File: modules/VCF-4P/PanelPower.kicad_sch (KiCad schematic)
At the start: 33 parts, among them J1 WQP-PJ398, J10 Conn_Front_Left, J11 Conn_Back_Right, J12 Conn_Front_Right, J13 Conn_Back_Left, J3 WQP-PJ398, J4 WQP-PJ398, J5 WQP-PJ398, J7 WQP-PJ398, J9 Conn_Eurorack_16, U2 TL074

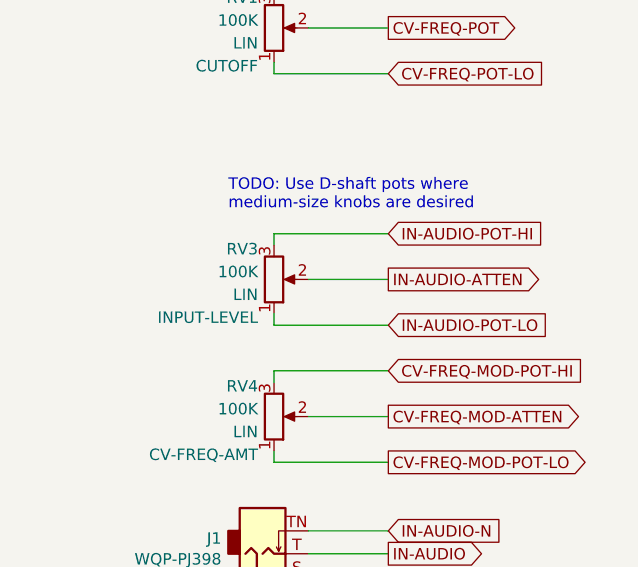
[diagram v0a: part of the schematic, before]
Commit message: VCF-4P: input level uses audio-taper pot
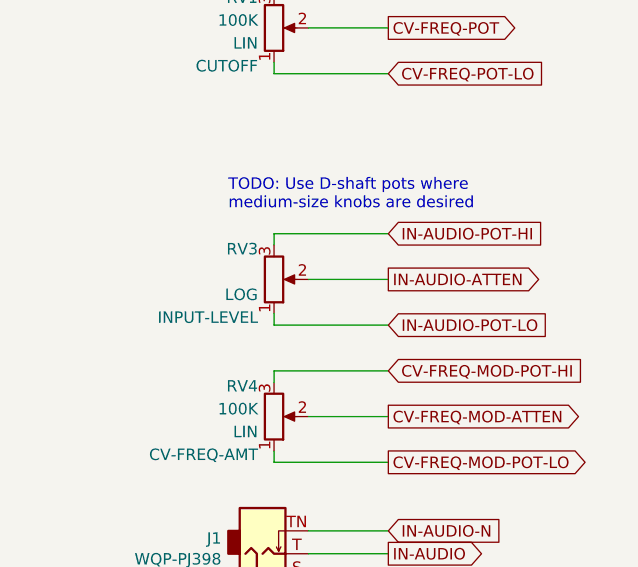
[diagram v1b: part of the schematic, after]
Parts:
- RV3: value 100K -> (none); footprint -lmp-synth:Potentiometer_Alpha_RD901F-40-00D_Single_Vertical -> (none); Value2 LIN -> LOG

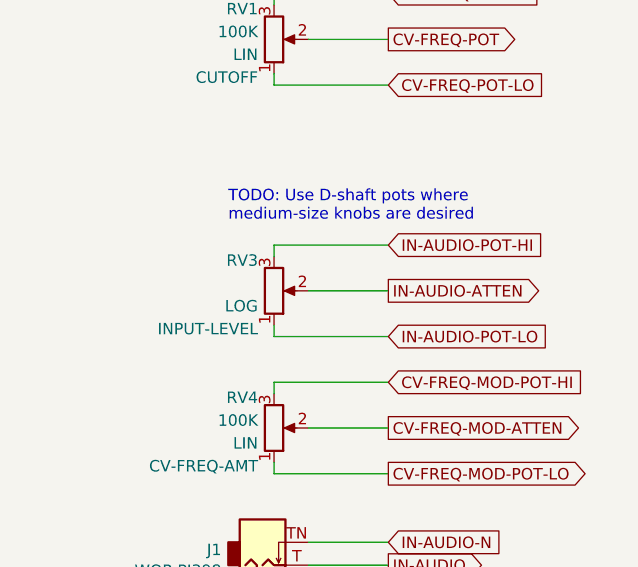
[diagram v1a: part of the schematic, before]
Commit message: VCF-4P: Breadboard prototype - wip
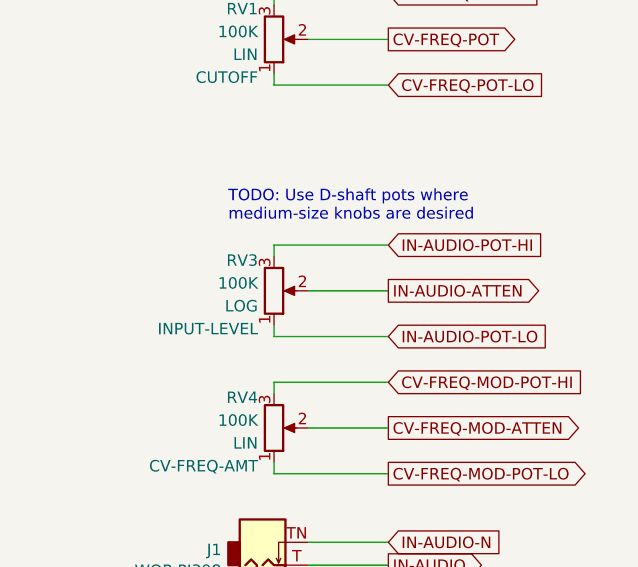
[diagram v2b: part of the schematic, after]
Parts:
- RV3: value (none) -> 100K; footprint (none) -> -lmp-synth:Potentiometer_Alpha_RD901F-40-00D_Single_Vertical

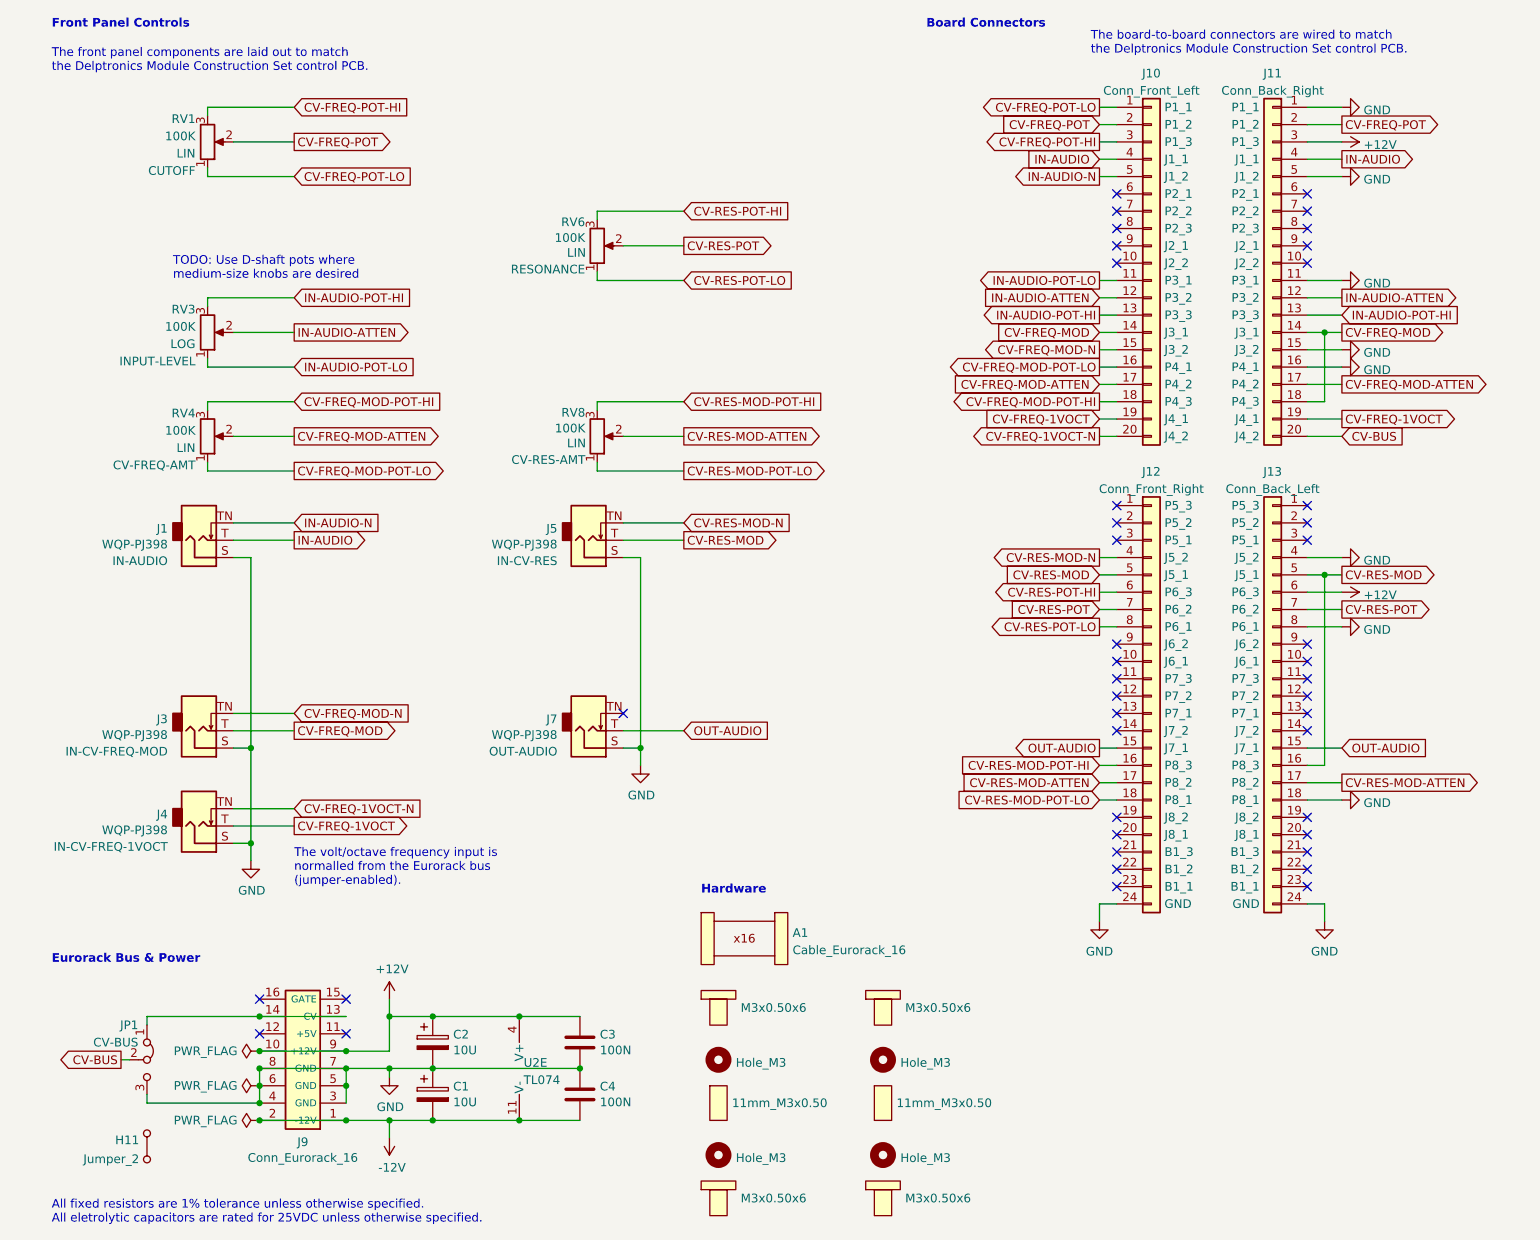
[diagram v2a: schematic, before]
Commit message: VCF-4P: Correct part numbers for DIP breakout version of SSI2140
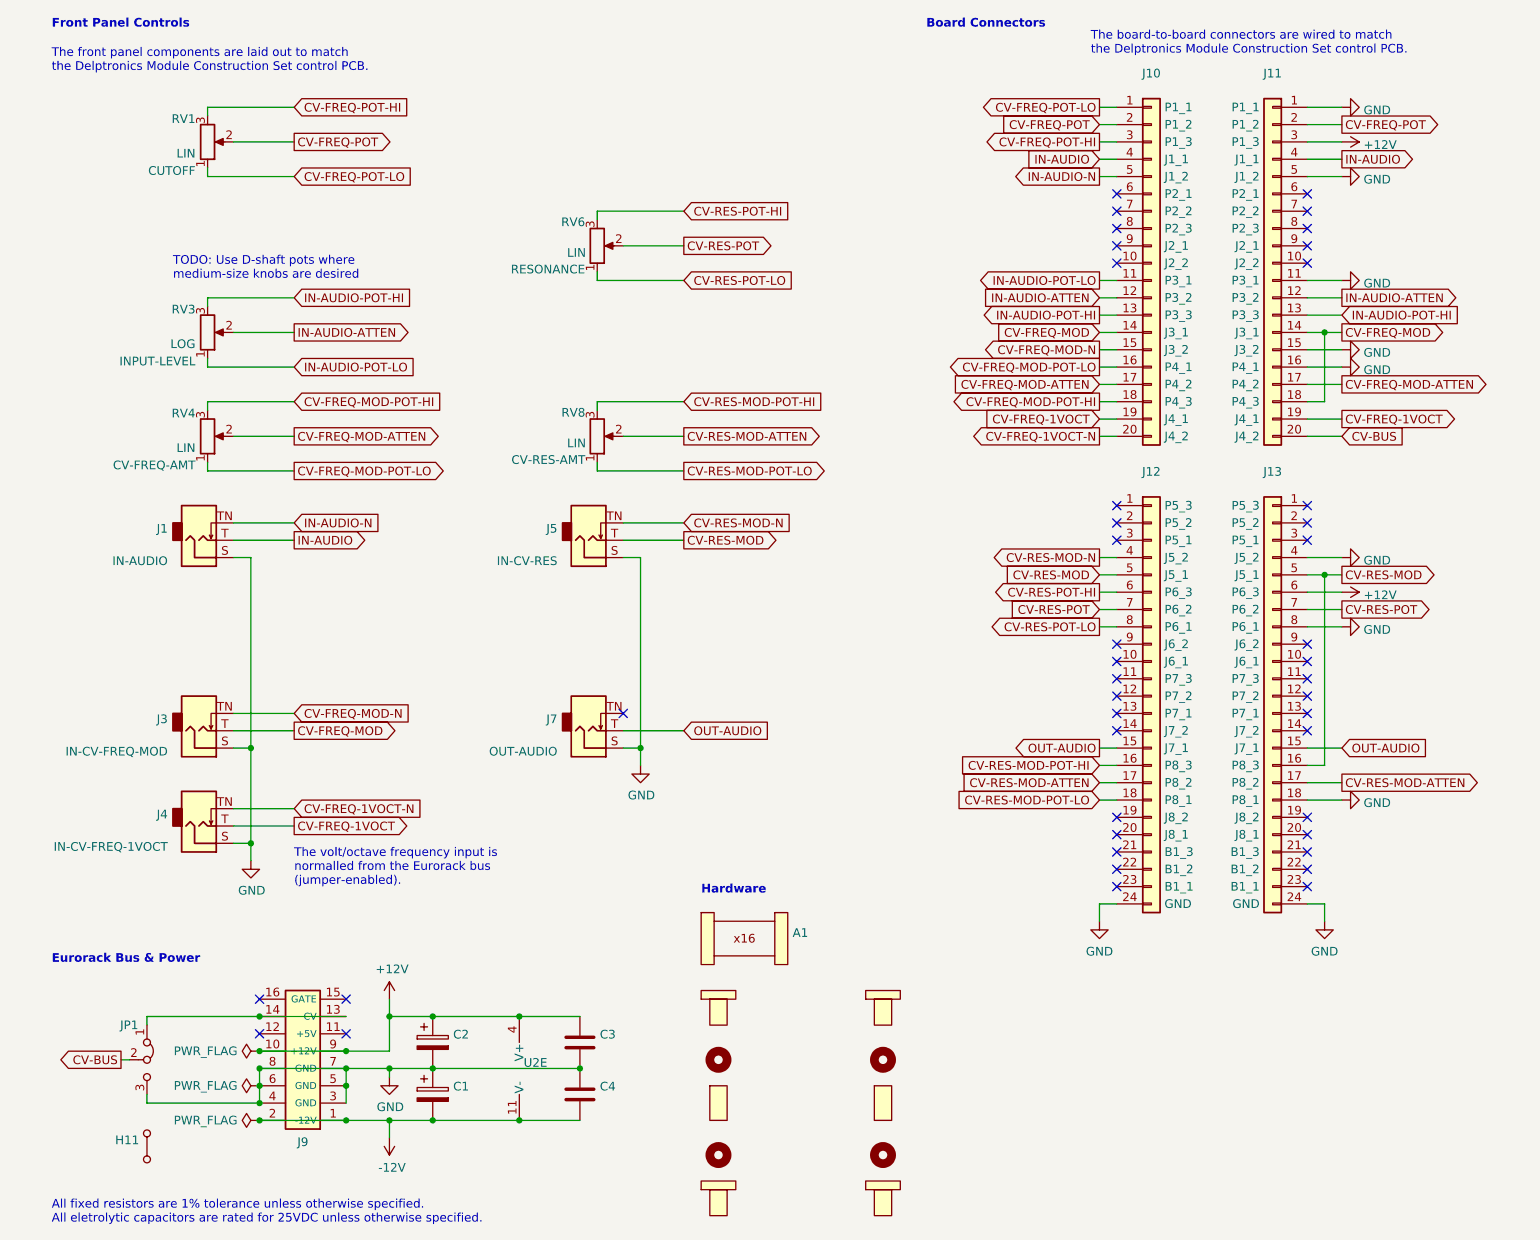
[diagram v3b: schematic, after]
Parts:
- A1: value Cable_Eurorack_16 -> (none); footprint -lmp-misc:NoFootprint -> (none)
- C1, C2: value 10U -> (none); footprint -lmp-misc:CP_Radial_D4.0mm_P1.50mm -> (none)
- C3, C4: value 100N -> (none); footprint -lmp-misc:C_Disc_D5.0mm_W2.5mm_P2.50mm -> (none)
- H1, H2, H3, H4: value Hole_M3 -> (none); footprint -lmp-holes:MountingHole_PCB_3.2mm_M3 -> (none)
- H10, H5, H7, H8: value M3x0.50x6 -> (none)
- H11: value Jumper_2 -> (none); footprint -lmp-misc:NoFootprint -> (none)
- H6, H9: value 11mm_M3x0.50 -> (none)
- J1, J3, J4, J5, J7: value WQP-PJ398 -> (none); footprint -lmp-synth:Jack_3.5mm_QingPu_WQP-PJ398SM_Vertical -> (none)
- J10: value Conn_Front_Left -> (none); footprint -lmp-synth:PinSocket_Delptronics_Front -> (none)
- J11: value Conn_Back_Right -> (none); footprint -lmp-synth:PinHeader_Delptronics_Back_8HP -> (none)
- J12: value Conn_Front_Right -> (none); footprint -lmp-synth:PinSocket_Delptronics_Front -> (none)
- J13: value Conn_Back_Left -> (none); footprint -lmp-synth:PinHeader_Delptronics_Back_8HP -> (none)
- J9: value Conn_Eurorack_16 -> (none); footprint -lmp-synth:IDC-Header-Eurorack-16-TH -> (none)
- JP1: value CV-BUS -> (none); footprint -lmp-misc:PinHeader_1x03_P2.54mm_Vertical -> (none)
- RV1, RV3, RV6: value 100K -> (none); footprint -lmp-synth:Potentiometer_Alpha_RD901F-40-00D_Single_Vertical -> (none)
- RV4, RV8: value 100K -> (none); footprint -lmp-synth:Potentiometer_SongHuei_Single_Vertical -> (none)
- U2: value TL074 -> (none); footprint Package_DIP:DIP-14_W7.62mm -> (none)

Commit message: VCF-4P: schematic tweaks
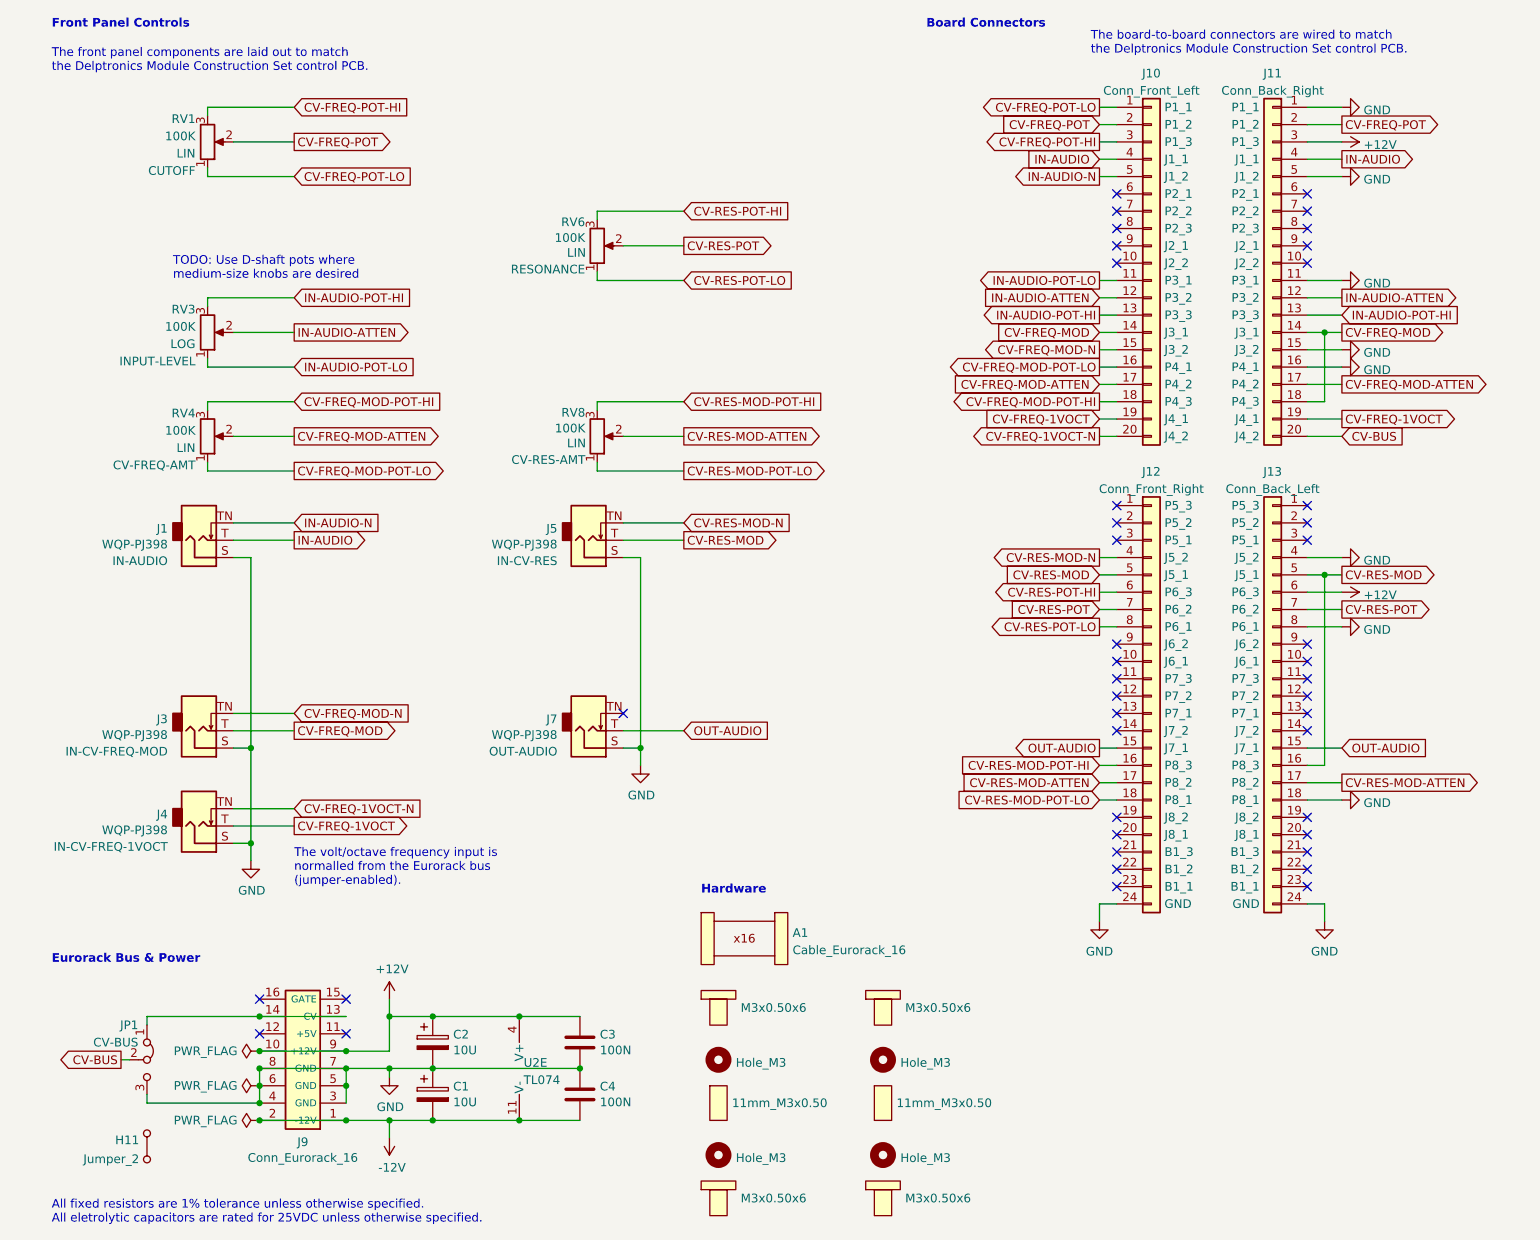
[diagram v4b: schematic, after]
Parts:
- A1: value (none) -> Cable_Eurorack_16; footprint (none) -> -lmp-misc:NoFootprint
- C1, C2: value (none) -> 10U; footprint (none) -> -lmp-misc:CP_Radial_D4.0mm_P1.50mm
- C3, C4: value (none) -> 100N; footprint (none) -> -lmp-misc:C_Disc_D5.0mm_W2.5mm_P2.50mm
- H1, H2, H3, H4: value (none) -> Hole_M3; footprint (none) -> -lmp-holes:MountingHole_PCB_3.2mm_M3
- H10, H5, H7, H8: value (none) -> M3x0.50x6
- H11: value (none) -> Jumper_2; footprint (none) -> -lmp-misc:NoFootprint
- H6, H9: value (none) -> 11mm_M3x0.50
- J1, J3, J4, J5, J7: value (none) -> WQP-PJ398; footprint (none) -> -lmp-synth:Jack_3.5mm_QingPu_WQP-PJ398SM_Vertical
- J10: value (none) -> Conn_Front_Left; footprint (none) -> -lmp-synth:PinSocket_Delptronics_Front
- J11: value (none) -> Conn_Back_Right; footprint (none) -> -lmp-synth:PinHeader_Delptronics_Back_8HP
- J12: value (none) -> Conn_Front_Right; footprint (none) -> -lmp-synth:PinSocket_Delptronics_Front
- J13: value (none) -> Conn_Back_Left; footprint (none) -> -lmp-synth:PinHeader_Delptronics_Back_8HP
- J9: value (none) -> Conn_Eurorack_16; footprint (none) -> -lmp-synth:IDC-Header-Eurorack-16-TH
- JP1: value (none) -> CV-BUS; footprint (none) -> -lmp-misc:PinHeader_1x03_P2.54mm_Vertical
- RV1, RV3, RV6: value (none) -> 100K; footprint (none) -> -lmp-synth:Potentiometer_Alpha_RD901F-40-00D_Single_Vertical
- RV4, RV8: value (none) -> 100K; footprint (none) -> -lmp-synth:Potentiometer_SongHuei_Single_Vertical
- U2: value (none) -> TL074; footprint (none) -> Package_DIP:DIP-14_W7.62mm

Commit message: VCF-4P - wip
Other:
- note added: "TODO: Can use Delptronics package? If so, add to BOM."
- note added: "TODO: front panel arrangement"

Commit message: VCF-4P - wip
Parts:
- removed H1, H2, H3: Hole_M3, -lmp-holes:MountingHole_PCB_3.2mm_M3, symbol -lmp-holes:MountingHole_PCB_M3
- removed H10, H8: M3x0.50x6, symbol -lmp-synth:HW_Screw_M3x0.50x6
- removed H9: 11mm_M3x0.50, symbol -lmp-synth:HW_Standoff_F-F_11mm_M3x0.50
- added H2: Delptronics_MCS_10HP, symbol -lmp-synth:PCB_Delptronics_MCS_10HP
- renumbered H11 to H1, H5 to H3, H7 to H4, H6 to H5, H4 to H6, J4 to J3, J3 to J5, J5 to J7, J7 to J8, RV4 to RV2, RV3 to RV4, RV6 to RV7
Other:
- note removed: "TODO: Can use Delptronics package? If so, add to BOM."
- note removed: "TODO: Use D-shaft pots where medium-size knobs are desired"
- note removed: "TODO: front panel arrangement"
- moved on the sheet: A1, C1, C2, C3, C4, H1, J1, J3, J5, J8, J9, JP1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

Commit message: VCF-4P: PCB layout - wip
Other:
- note added: "The front panel and the board-to-board connectors are laid out to match the Delptronics Module Construction Set control PCB."
- note removed: "The board-to-board connectors are wired to match the Delptronics Module Construction Set control PCB."
- note removed: "The front panel components are laid out to match the Delptronics Module Construction Set control PCB."

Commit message: VCF-4P: PCB layout - wip
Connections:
- net GND: now also JP1.1 (A); no longer JP1.3 (B)
- net at J9.13 (CV), J9.14: now also JP1.3 (B); no longer JP1.1 (A)
